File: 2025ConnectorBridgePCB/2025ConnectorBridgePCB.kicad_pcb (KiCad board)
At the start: 2 copper layers, 135 x 71 mm, 9 parts, among them J1 DA15_Socket, J2 DA15_Socket, J3 Conn_01x03_Socket, J4 Conn_01x05_Socket, J5 Conn_01x03_Socket, J6 Conn_01x05_Socket, J7 Conn_01x03_Socket, P1 USB_C_Plug_USB2.0, U1 MCP2551-I-SN

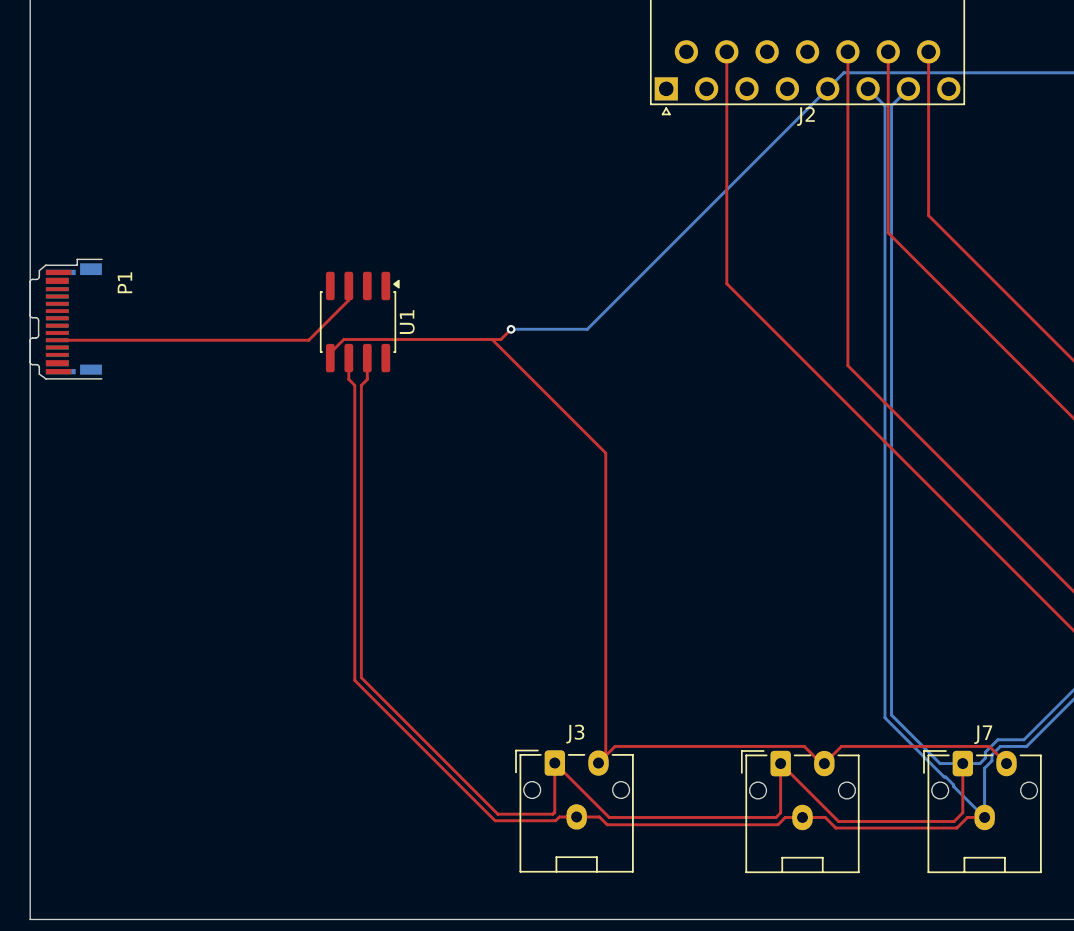
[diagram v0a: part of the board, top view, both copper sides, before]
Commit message: Replace USB/MCP2515 with daughter board thru hole idea
We were discussing at one point soldering on a daughter board  that houses USB CAN functionality. We can make a branch for onboard USB-CAN functionality
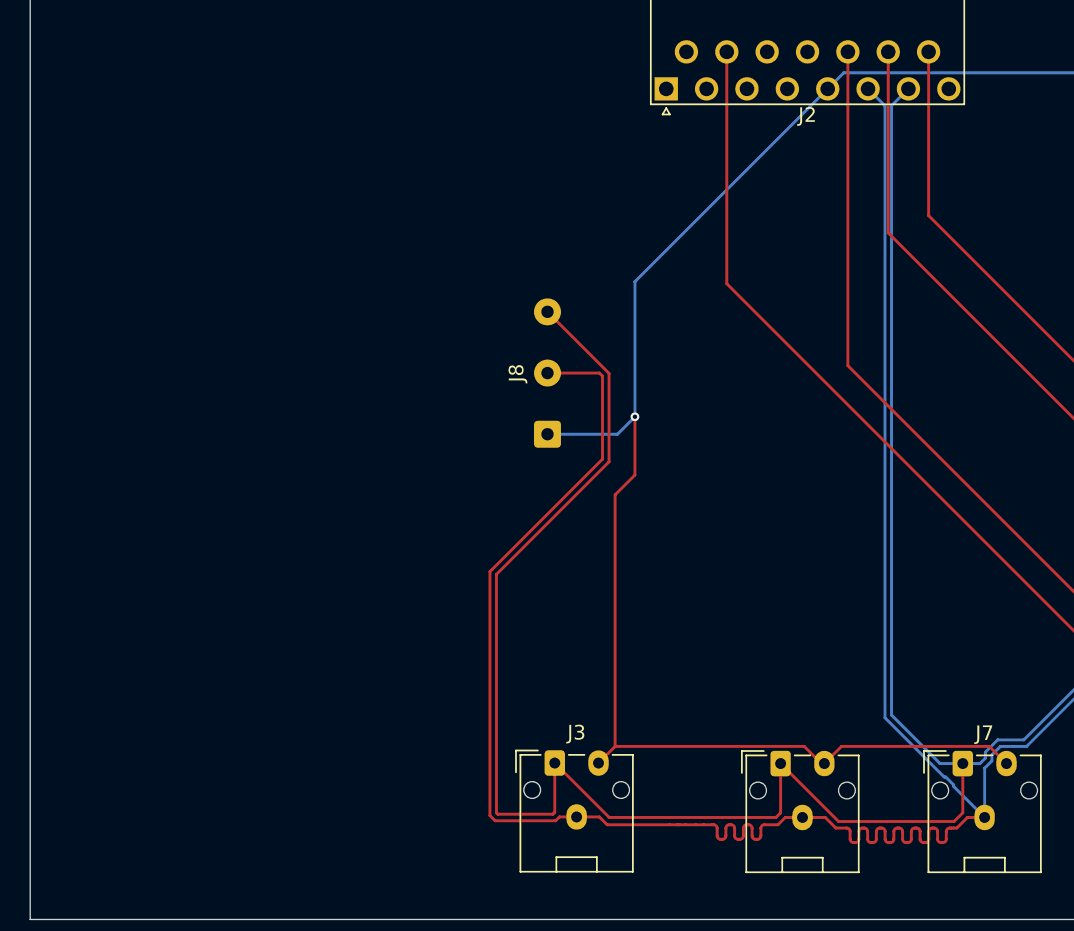
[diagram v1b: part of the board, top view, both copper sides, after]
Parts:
- removed P1: USB_C_Plug_USB2.0, Connector_USB:USB_C_Plug_JAE_DX07P024AJ1
- removed U1: MCP2551-I-SN, Package_SO:SOIC-8_3.9x4.9mm_P1.27mm
- added J8: Conn_01x03_Socket, Connector_Wire:SolderWire-0.25sqmm_1x03_P4.2mm_D0.65mm_OD1.7mm, F.Cu at (103.5, 92.7)
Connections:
- net CANV renamed GND
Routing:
- net Net-(U1-VDD): track 22.1 -> 0.00 mm
- net GND: track 162.8 -> 146.0 mm
- net CAN-: track 195.5 -> 211.3 mm
- net CAN+: track 204.1 -> 208.2 mm

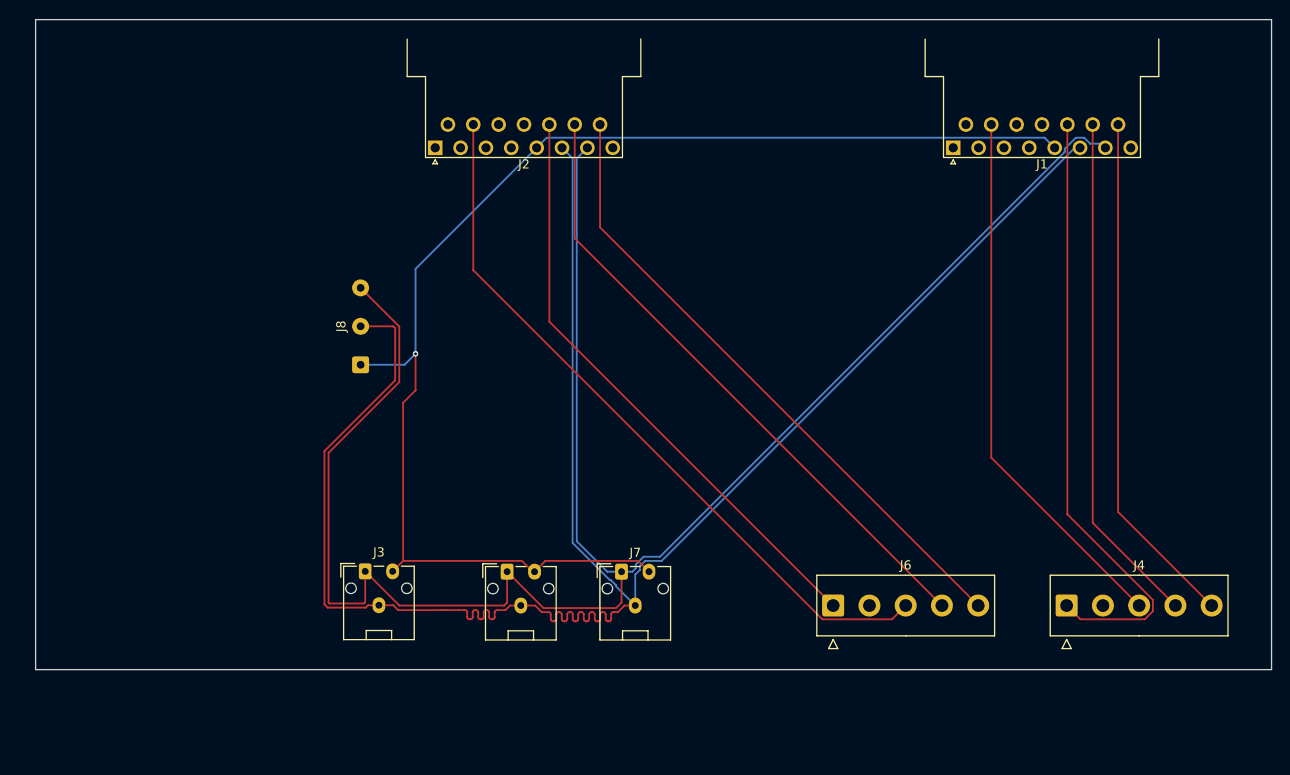
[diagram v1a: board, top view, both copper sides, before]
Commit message: Shrink Everything, Use proper Encoder Connectors
This also adds a screw terminal, not wired up yet but it will breakout unused pins from DB15.
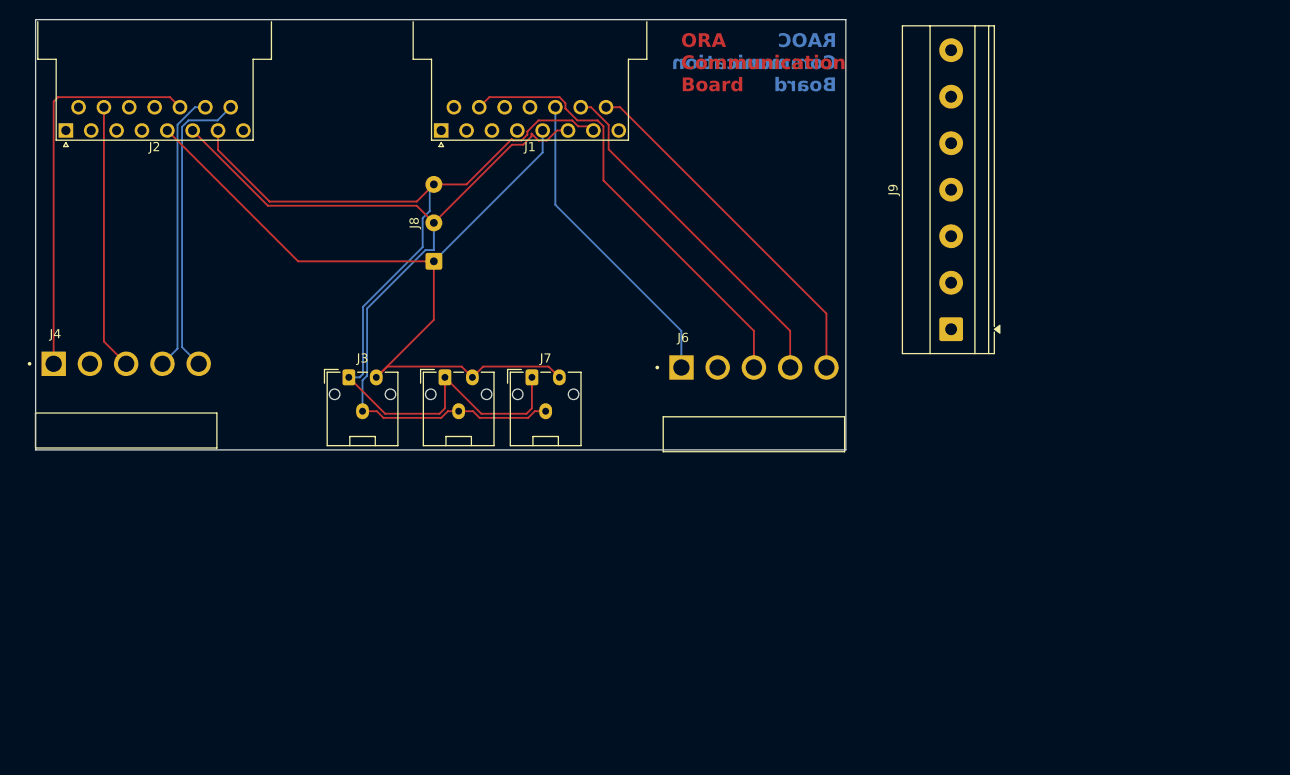
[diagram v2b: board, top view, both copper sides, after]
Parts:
- added J9: Screw_Terminal_01x07, TerminalBlock_Phoenix:TerminalBlock_Phoenix_MKDS-1,5-7-5.08_1x07_P5.08mm_Horizontal, F.Cu at (168.0, 88.8)
- J4, J6: value Conn_01x05_Socket -> 640389-5; footprint Connector_TE-Connectivity:TE_826576-5_1x05_P3.96mm_Vertical -> 640389-5:TE_640389-5
- moved J4 113.8 mm to (70.0, 92.6)
- moved J1 56.0 mm to (112.3, 67.1)
- moved J2 40.4 mm to (71.3, 67.1)
- moved J6 30.8 mm to (138.5, 93.0)
- moved J7 23.4 mm to (122.2, 94.1)
- moved J5 22.3 mm to (112.7, 94.1)
- moved J3 21.3 mm to (102.2, 94.1)
- moved J8 13.8 mm to (111.5, 81.4)
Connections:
- J1 pad 1: unconnected-(J1-Pad1) -> MOT_B_DOUT1
- J1 pad 11: unconnected-(J1-P111-Pad11) -> MOT_B_ANACMD
- J1 pad 12: unconnected-(J1-P12-Pad12) -> MOT_B_DIN3
- J1 pad 2: unconnected-(J1-Pad2) -> MOT_B_TX
- J1 pad 3: unconnected-(J1-Pad3) -> MOT_B_RX
- J1 pad 4: unconnected-(J1-Pad4) -> MOT_B_RCRADIO
- J1 pad 8: unconnected-(J1-Pad8) -> MOT_B_DIN2
- J1 pad 9: unconnected-(J1-P9-Pad9) -> MOT_B_DOUT2
- J2 pad 1: unconnected-(J2-Pad1) -> MOT_A_DOUT1
- J2 pad 11: unconnected-(J2-P111-Pad11) -> MOT_A_ANACMD
- J2 pad 12: unconnected-(J2-P12-Pad12) -> MOT_A_DIN3
- J2 pad 2: unconnected-(J2-Pad2) -> MOT_A_TX
- J2 pad 3: unconnected-(J2-Pad3) -> MOT_A_RX
- J2 pad 4: unconnected-(J2-Pad4) -> MOT_A_RCRADIO
- J2 pad 8: unconnected-(J2-Pad8) -> MOT_A_DIN2
- J2 pad 9: unconnected-(J2-P9-Pad9) -> MOT_A_DOUT2
- J4 pad 1: MOT_B_GND -> MOT_A_GND
- J4 pad 3: MOT_B_ENCA -> MOT_A_ENCA
- J4 pad 4: MOT_B_5VOUT -> MOT_A_5VOUT
- J4 pad 5: MOT_B_ENCB -> MOT_A_ENCB
- J6 pad 1: MOT_A_GND -> MOT_B_GND
- J6 pad 3: MOT_A_ENCA -> MOT_B_ENCA
- J6 pad 4: MOT_A_5VOUT -> MOT_B_5VOUT
- J6 pad 5: MOT_A_ENCB -> MOT_B_ENCB
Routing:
- net CAN-: track 211.3 -> 95.7 mm
- net CAN+: track 208.2 -> 106.7 mm
- net GND: track 146.0 -> 91.5 mm, vias 1 -> 0
- net MOT_A_ENCA: track 79.9 -> 29.0 mm
- net MOT_A_5VOUT: track 69.5 -> 30.6 mm
- net MOT_A_ENCB: track 69.9 -> 32.8 mm
- net MOT_B_GND: track 67.7 -> 34.1 mm
- net MOT_A_GND: track 65.7 -> 43.1 mm
- net MOT_B_5VOUT: track 56.6 -> 38.6 mm
- net MOT_B_ENCB: track 57.1 -> 39.3 mm
- net MOT_B_ENCA: track 59.5 -> 48.8 mm
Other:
- board size 135 x 71 mm -> 88.5 x 47 mm
- board text added: "ORA Communication Board"
- board text added: "RAOC Communication Board"

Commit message: Proper connectors
Use proper connectors for CAN, Encoders, and DB-15. Breakout unused DB-15 pads to screw terminals.
Also added mounting holes but did not fillet corners yet in case dimensions need to be changed.
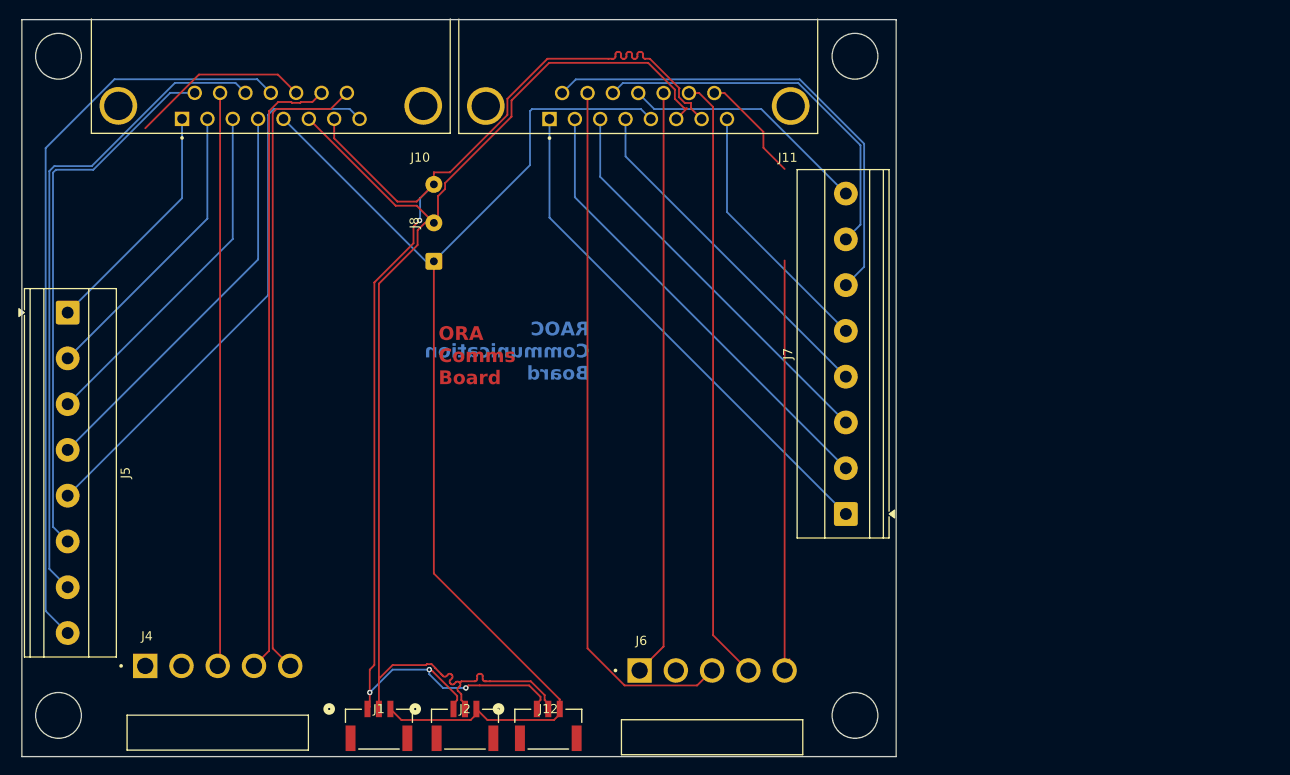
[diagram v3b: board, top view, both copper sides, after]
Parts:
- removed J3: Conn_01x03_Socket, Connector_JST:JST_ZE_S03B-ZESK-2D_1x03_P1.50mm_Horizontal
- removed J9: Screw_Terminal_01x07, TerminalBlock_Phoenix:TerminalBlock_Phoenix_MKDS-1,5-7-5.08_1x07_P5.08mm_Horizontal
- added J10: L77SDA15SA4CH4F, L77SDA15SA4CH4F:AMPHENOL_L77SDA15SA4CH4F, F.Cu at (93.7, 64.4)
- added J11: L77SDA15SA4CH4F, L77SDA15SA4CH4F:AMPHENOL_L77SDA15SA4CH4F, F.Cu at (133.8, 64.4)
- added J12: SM03B-GHS-TBLFSN, SM03B_GHS_TB_LF__SN_:CONN_SM03B-GHS-TBLFSN_JST, F.Cu at (124.0, 132.5)
- J1, J2: value DA15_Socket -> SM03B-GHS-TBLFSN; footprint Connector_Dsub:DSUB-15_Socket_Horizontal_P2.77x2.54mm_EdgePinOffset9.40mm -> SM03B_GHS_TB_LF__SN_:CONN_SM03B-GHS-TBLFSN_JST
- J5, J7: value Conn_01x03_Socket -> Screw_Terminal_01x08; footprint Connector_JST:JST_ZE_S03B-ZESK-2D_1x03_P1.50mm_Horizontal -> TerminalBlock_Phoenix:TerminalBlock_Phoenix_MKDS-1,5-8_1x08_P5.00mm_Horizontal
- moved J2 78.6 mm to (114.9, 132.5), turned to 0 degrees
- moved J1 65.7 mm to (105.5, 132.5), turned to 0 degrees
- moved J5 41.8 mm to (71.5, 87.0), turned to -90 degrees
- moved J7 37.4 mm to (156.5, 109.0), turned to 90 degrees
- moved J4 34.5 mm to (80.0, 125.6)
- moved J6 33.4 mm to (134.0, 126.1)
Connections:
- J1 pad 1: MOT_B_DOUT1 -> CAN+
- J1 pad 2: MOT_B_TX -> CAN-
- J1 pad 3: MOT_B_RX -> GND
- J1 pad 4: MOT_B_RCRADIO -> (no net)
- J1 pad 5: GND -> (no net)
- J2 pad 1: MOT_A_DOUT1 -> CAN+
- J2 pad 2: MOT_A_TX -> CAN-
- J2 pad 3: MOT_A_RX -> GND
- J2 pad 4: MOT_A_RCRADIO -> (no net)
- J2 pad 5: GND -> (no net)
- J5 pad 1: CAN+ -> MOT_A_DOUT1
- J5 pad 2: CAN- -> MOT_A_TX
- J5 pad 3: GND -> MOT_A_RX
- J7 pad 1: CAN+ -> MOT_B_DOUT1
- J7 pad 2: CAN- -> MOT_B_TX
- J7 pad 3: GND -> MOT_B_RX
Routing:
- net MOT_A_DIN3: track 0.00 -> 82.3 mm
- net MOT_A_ANACMD: track 0.00 -> 72.1 mm
- net MOT_A_DIN2: track 0.00 -> 61.4 mm
- net MOT_A_DOUT2: track 0.00 -> 60.0 mm
- net MOT_B_DOUT1: track 0.00 -> 56.6 mm
- net MOT_B_DOUT2: track 0.00 -> 52.8 mm
- net MOT_B_TX: track 0.00 -> 50.4 mm
- net CAN-: track 95.7 -> 144.3 mm
- net MOT_A_RCRADIO: track 0.00 -> 44.8 mm
- net MOT_B_RX: track 0.00 -> 44.3 mm
- net CAN+: track 106.7 -> 150.0 mm, vias 0 -> 4
- net GND: track 91.5 -> 133.7 mm
- net MOT_B_ANACMD: track 0.00 -> 41.2 mm
- net MOT_A_RX: track 0.00 -> 38.6 mm
- net MOT_B_RCRADIO: track 0.00 -> 38.1 mm
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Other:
- board size 88.5 x 47 mm -> 95.5 x 80.5 mm
- board text added: "ORA Comms Board"
- board text removed: "ORA Communication Board"

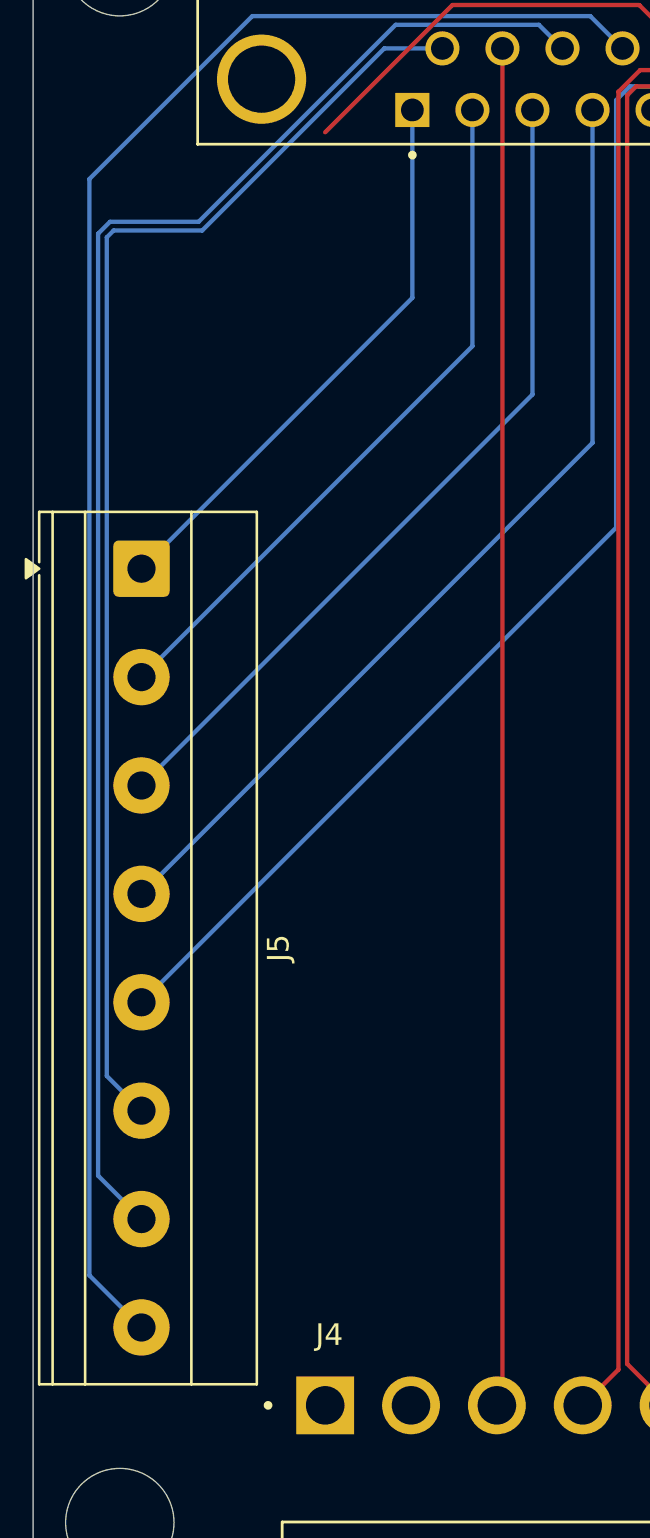
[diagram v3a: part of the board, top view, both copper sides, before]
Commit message: Comm Board: Fix Missing Connection
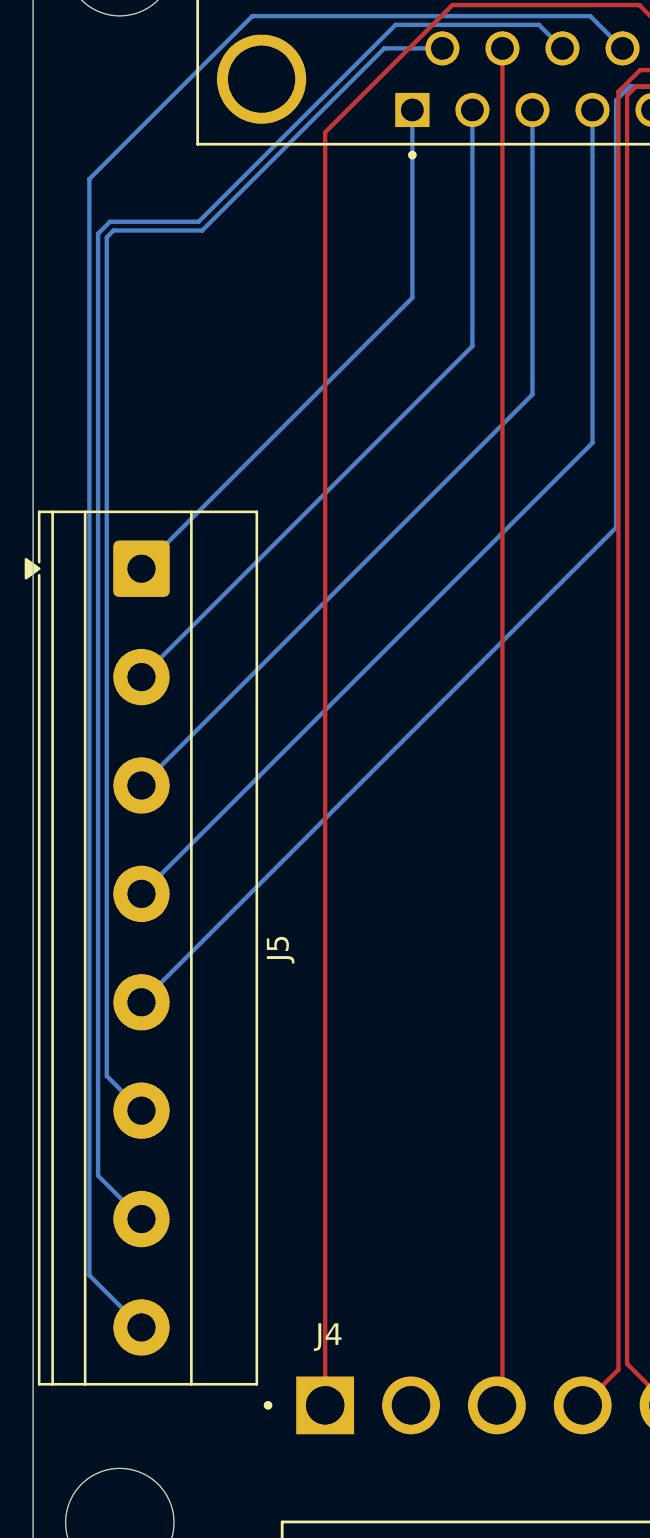
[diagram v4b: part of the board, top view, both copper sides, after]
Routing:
- net MOT_A_GND: track 19.7 -> 78.5 mm
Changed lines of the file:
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@@
+	)
+	(segment
+		(start 79.97325 66.867378)
+		(end 79.97325 125.5925)
+		(width 0.2)
+		(layer "F.Cu")
+		(net 10)
 	)
 	(segment
